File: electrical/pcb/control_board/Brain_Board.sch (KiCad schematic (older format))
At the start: 37 parts, among them J10 6posheader, J27 PEC10DAAN, J32 PPTC021LFBN-RC, J45 PPTC021LFBN-RC, J46 PPTC021LFBN-RC, J6 S9175-ND_rpi_breakout, J67 PPTC041LFBN-RC, J7 S9175-ND_rpi_breakout, Q1 2N3906, Q2 2N3906, Q3 2N3906, SW1 SW_SPDT, SW2 SW_SPDT, SW3 SW_SPDT

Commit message: Updates from conversation on Dec 16
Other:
- note added: "TODO: change these switches over to https://www.digikey.com/en/products/detail/nkk-switches/JS0104AP4-S/2104258"
- note added: "TODO: check logic here, make sure it’s what we want"
- note added: "Todo: make 3x4 header - 4 redundant rows"
- note added: "Todo: make the two 3.3v nets have the same name"
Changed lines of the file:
@@
 EESchema Schematic File Version 4
-LIBS:Control_Boards-cache
-EELAYER 26 0
+EELAYER 30 0
 EELAYER END
 $Descr A4 11693 8268
@@
 L JPL_Robotics_Lib:PPTC041LFBN-RC J67
 U 1 1 61023155
-P 5150 6150
-F 0 "J67" H 5278 6275 39  0000 L CNN
-F 1 "PPTC041LFBN-RC" H 5200 6500 50  0001 C CNN
-F 2 "JPL Robotics:PPTC041LFBN-RC" H 5300 6350 50  0001 C CNN
-F 3 "" H 5300 6350 50  0001 C CNN
-	1    5150 6150
-	1    0    0    -1
-$EndComp
-Wire Wire Line
-	5050 5950 4850 5950
-Text Label 4850 5950 0    30   ~ 0
+P 4900 5950
+F 0 "J67" H 5028 6075 39  0000 L CNN
+F 1 "PPTC041LFBN-RC" H 4950 6300 50  0001 C CNN
+F 2 "JPL Robotics:PPTC041LFBN-RC" H 5050 6150 50  0001 C CNN
+F 3 "" H 5050 6150 50  0001 C CNN
+	1    4900 5950
+	1    0    0    -1
+$EndComp
+Wire Wire Line
+	4800 5750 4600 5750
+Text Label 4600 5750 0    30   ~ 0
 SDA_rpi
 Wire Wire Line
-	5050 6000 4850 6000
-Text Label 4850 6000 0    30   ~ 0
+	4800 5800 4600 5800
+Text Label 4600 5800 0    30   ~ 0
 SCL_rpi
 Wire Wire Line
-	5050 6050 4850 6050
-Text Label 4850 6050 0    30   ~ 0
-GND
-NoConn ~ 5050 6100
+	4800 5850 4600 5850
+Text Label 4600 5850 0    30   ~ 0
+GND
+NoConn ~ 4800 5900
 Wire Notes Line
 	4450 5350 4450 6450
@@
 Text Notes 9200 1300 0    31   ~ 0
 - Roboclaw ESTOPs active low \n(emergency stop when pulled low)\n- LEDs off when estop’ed (nominal on)
+Text Notes 2100 1650 0    31   ~ 0
+Todo: make the two 3.3v nets have the same name
+Text Notes 4750 6150 0    31   ~ 0
+Todo: make 3x4 header - 4 redundant rows
+Text Notes 7100 1100 0    31   ~ 0
+TODO: check logic here, make sure it’s what we want
+Text Notes 7150 950  0    31   ~ 0
+TODO: change these switches over to https://www.digikey.com/en/products/detail/nkk-switches/JS0104AP4-S/2104258
+Text Notes 7200 5100 0    31   ~ 0
+TODO: check logic here, make sure it’s what we want
 $EndSCHEMATC

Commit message: Updating molex connector footprint, changing rpi i2c header to 3x4, and consolidating switches to a 4 SPDT DIP packages
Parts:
- removed J67: PPTC041LFBN-RC, JPL Robotics:PPTC041LFBN-RC, symbol JPL_Robotics_Lib:PPTC041LFBN-RC
- removed SW1, SW2, SW3: SW_SPDT, symbol Switch:SW_SPDT
- added J14: CTS-206-124, symbol JPL_Robotics_Lib:CTS-206-124
- added J67: SSW-104-01-F-T, symbol JPL_Robotics_Lib:SSW-104-01-F-T
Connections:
- wire segments 144 -> 169
- no-connect marks 50 -> 52
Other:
- note added: "4 redundant i2c \nconnections, for \ntalking to arbitrary \nperipherals"
- note removed: "TODO: change these switches over to https://www.digikey.com/en/products/detail/nkk-switches/JS0104AP4-S/2104258"
- note removed: "Todo: make 3x4 header - 4 redundant rows"
- moved on the sheet: D6, D7, D8, R53, R54, R55, R59, R60, R61

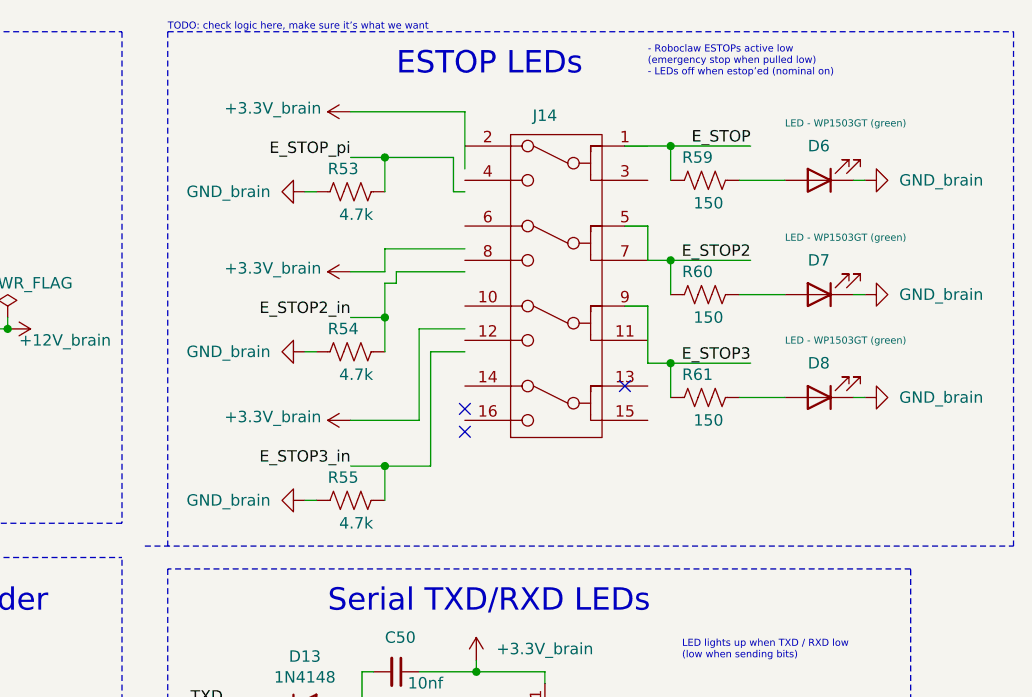
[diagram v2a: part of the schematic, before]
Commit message: Adding SSW-104-01-F-T and CTS-206-124 footprints
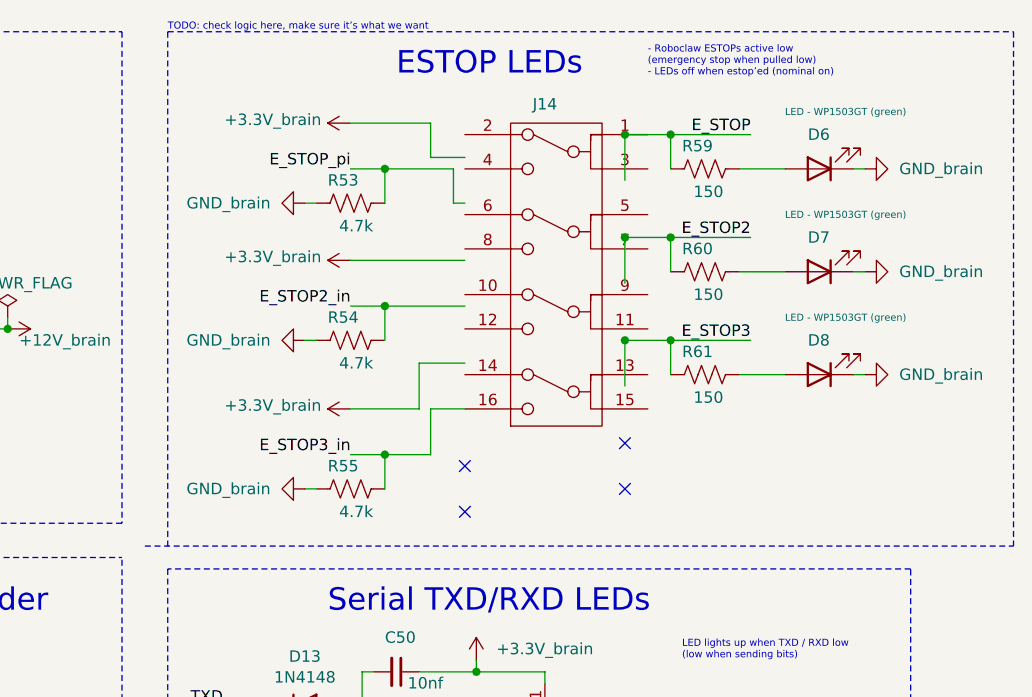
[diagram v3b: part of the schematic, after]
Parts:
- J67: footprint (none) -> JPL Robotics:SSW-104-01-F-T
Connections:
- wire segments 169 -> 164
- no-connect marks 52 -> 53
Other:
- moved on the sheet: D6, D7, D8, J14, R53, R54, R55, R59, R60, R61

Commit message: Small footprint updates
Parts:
- J14: footprint (none) -> JPL Robotics:CTS-206-124
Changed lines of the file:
@@
 F 0 "J14" H 8750 4483 50  0000 C CNN
 F 1 "CTS-206-124" H 8750 4484 50  0001 C CNN
-F 2 "" H 8600 2950 50  0001 C CNN
+F 2 "JPL Robotics:CTS-206-124" H 8600 2950 50  0001 C CNN
 F 3 "" H 8600 2950 50  0001 C CNN
 	1    8600 2950

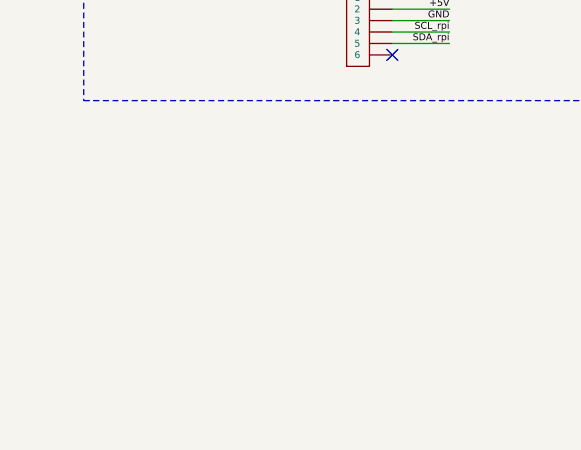
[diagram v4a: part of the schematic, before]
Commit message: Moving rpi mounting holes to brain board
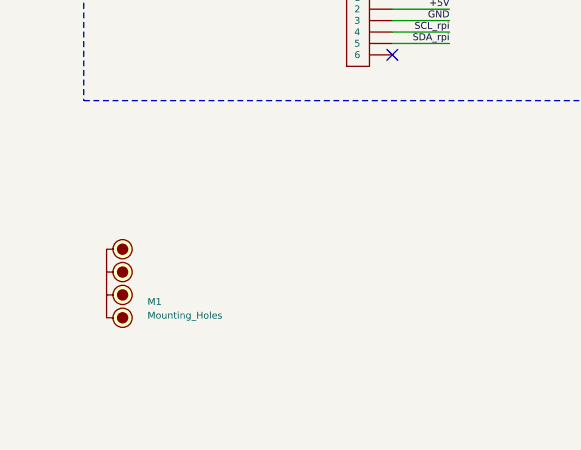
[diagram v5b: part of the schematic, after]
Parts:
- added M1: Mounting_Holes, JPL Robotics:Raspberry pi footprint, symbol JPL_Robotics_Lib:Mounting_Holes
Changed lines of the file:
@@
 	9100 2450 9100 2650
 Connection ~ 9100 2450
+$Comp
+L JPL_Robotics_Lib:Mounting_Holes M?
+U 1 1 61DB5332
+P 1550 6150
+AR Path="/60A51BAC/61DB5332" Ref="M?"  Part="1"
+AR Path="/60A5279E/61DB5332" Ref="M1"  Part="1"
+F 0 "M1" V 1980 6329 30  0000 L CNN
+F 1 "Mounting_Holes" V 2040 6329 30  0000 L CNN
+F 2 "JPL Robotics:Raspberry pi footprint" H 1730 6330 30  0001 C CNN
+F 3 "" H 1730 6330 30  0001 C CNN
+	1    1550 6150
+	0    1    1    0
+$EndComp
 $EndSCHEMATC

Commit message: CB updates from 1/6/2022 meeting
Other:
- note added: "TODO: make this schematic symbol less stupid\n\nUse actual switch symbols inside there, and show the connections from pins\n\nChange J to SW"
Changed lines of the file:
@@
 	0    1    1    0
 $EndComp
+Text Notes 9450 3050 0    31   ~ 0
+TODO: make this schematic symbol less stupid\n\nUse actual switch symbols inside there, and show the connections from pins\n\nChange J to SW
 $EndSCHEMATC

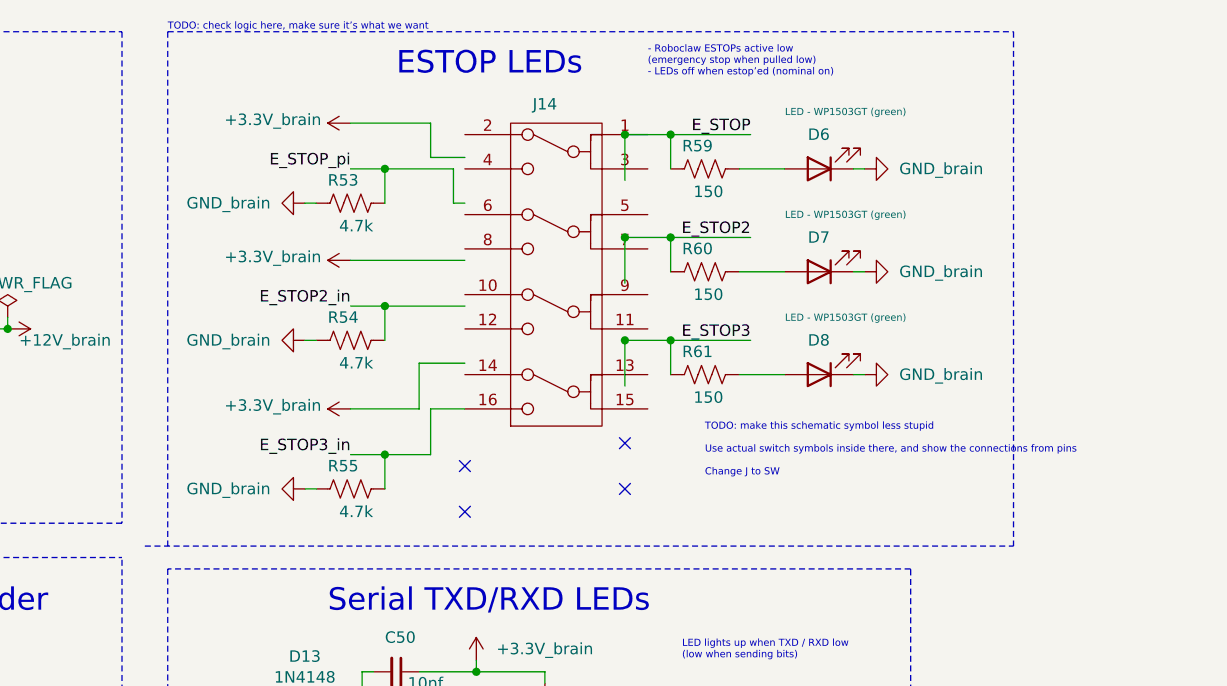
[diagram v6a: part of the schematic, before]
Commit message: Updating SPDT switch array symbol
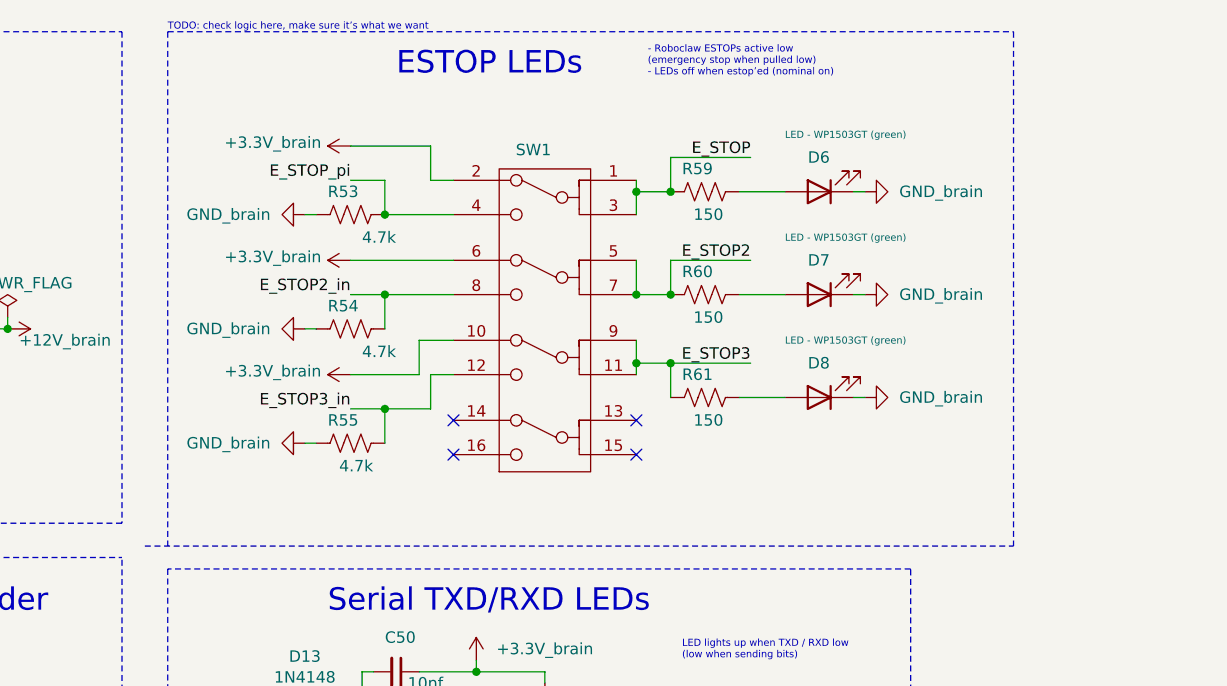
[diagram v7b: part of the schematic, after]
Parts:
- renumbered J14 to SW1
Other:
- note removed: "TODO: make this schematic symbol less stupid\n\nUse actual switch symbols inside there, and show the connections from pins\n\nChange J to SW"
- moved on the sheet: D6, D7, D8, R53, R54, R55, R59, R60, R61, SW1

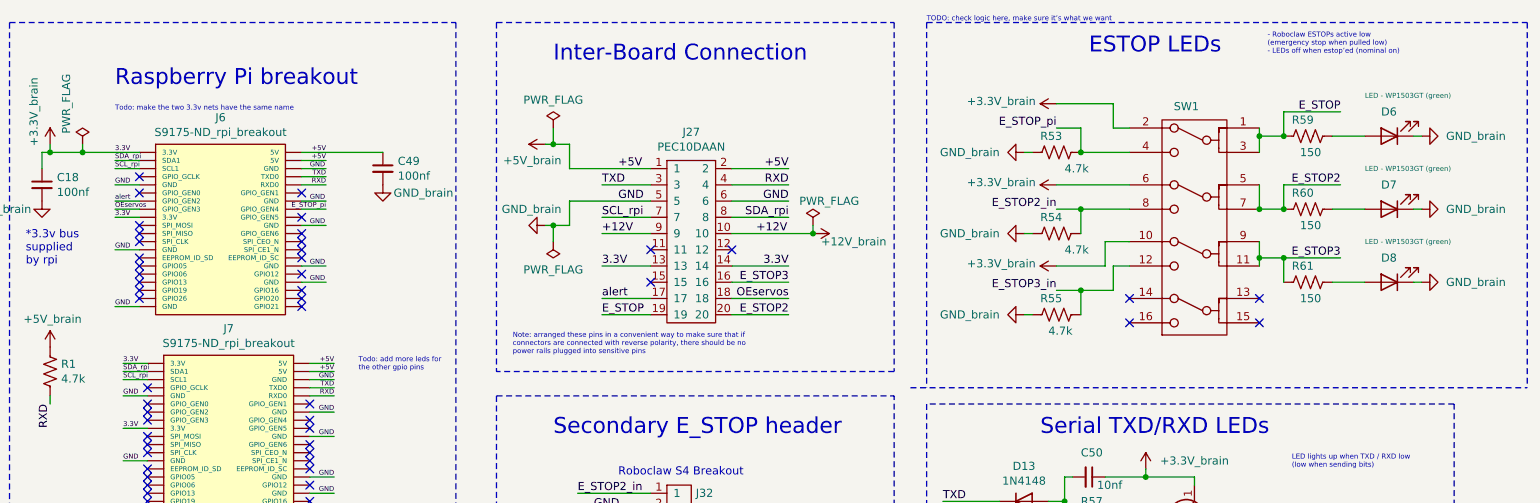
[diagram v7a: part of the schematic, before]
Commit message: Board updates from 2/3/2022 meeting
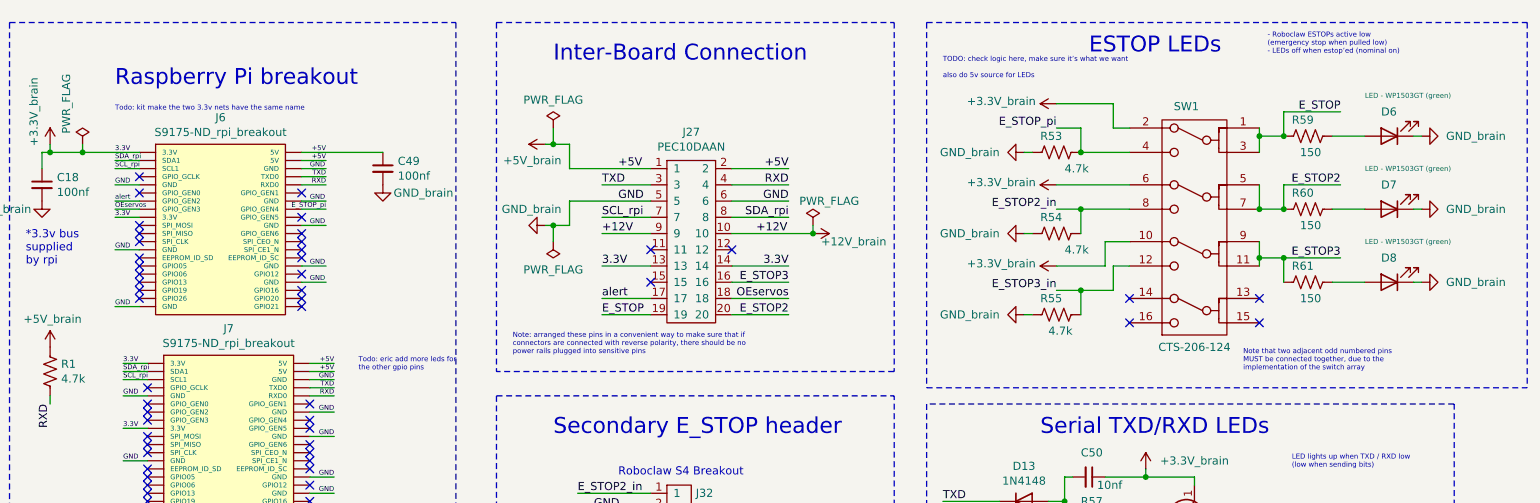
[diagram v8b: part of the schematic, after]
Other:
- note added: "Note that two adjacent odd numbered pins \nMUST be connected together, due to the \nimplementation of the switch array"
- note added: "TODO: check logic here, make sure it’s what we want\n\nalso do 5v source for LEDs"
- note added: "Todo: eric add more leds for \nthe other gpio pins"
- note added: "Todo: kit make the two 3.3v nets have the same name"
- note removed: "Todo: add more leds for \nthe other gpio pins"
- note removed: "Todo: make the two 3.3v nets have the same name"
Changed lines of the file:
@@
 	9600 2700 9800 2700
 Text Notes 3600 3250 0    31   ~ 0
-Todo: add more leds for \nthe other gpio pins
+Todo: eric add more leds for \nthe other gpio pins
 $Comp
 L JPL_Robotics_Lib:+3.3V_brain #PWR09
@@
 - Roboclaw ESTOPs active low \n(emergency stop when pulled low)\n- LEDs off when estop’ed (nominal on)
 Text Notes 2100 1650 0    31   ~ 0
-Todo: make the two 3.3v nets have the same name
-Text Notes 7100 1100 0    31   ~ 0
-TODO: check logic here, make sure it’s what we want
+Todo: kit make the two 3.3v nets have the same name
+Text Notes 7200 1450 0    31   ~ 0
+TODO: check logic here, make sure it’s what we want\n\nalso do 5v source for LEDs
 Text Notes 7200 5100 0    31   ~ 0
 TODO: check logic here, make sure it’s what we want
@@
 	10800 1100 10800 3350
 Wire Notes Line
-	7000 3350 10800 3350
-Wire Notes Line
 	7100 1100 10800 1100
 Wire Wire Line
@@
 P 8550 3150
 F 0 "SW1" H 8700 4683 50  0000 C CNN
-F 1 "CTS-206-124" H 8700 4684 50  0001 C CNN
+F 1 "CTS-206-124" H 8750 3200 50  0000 C CNN
 F 2 "JPL Robotics:CTS-206-124" H 8550 3150 50  0001 C CNN
 F 3 "" H 8550 3150 50  0001 C CNN
@@
 	9150 2550 9150 2600
 Connection ~ 9300 2550
+Wire Notes Line
+	7100 3350 10800 3350
+Text Notes 9050 3250 0    31   ~ 0
+Note that two adjacent odd numbered pins \nMUST be connected together, due to the \nimplementation of the switch array
 $EndSCHEMATC
